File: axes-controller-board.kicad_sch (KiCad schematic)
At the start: 76 parts, among them IC1 TPS5450QDDARQ1, J10 Conn_01x08, J11 Conn_01x04, J12 Conn_01x08, J13 Conn_01x04, J14 Conn_01x08, J15 Conn_01x08, J16 Conn_01x04, J17 Conn_01x08, J18 Conn_01x08, J19 Conn_01x04, J2 Conn_01x03, J20 Conn_01x08, J21 Conn_01x08, J22 Conn_01x04, J23 Conn_01x08, J24 Conn_01x08, J25 Conn_01x04, J26 Conn_01x08, J27 Raspberry_Pi_2_3, J28 DC1, J29 DC2, J3 Conn_01x03, J30 DC3, J31 Conn_01x08, J32 Conn_01x08, J33 DC1, J34 Conn_01x08, J35 Conn_01x08, J36 Conn_01x08, J37 ENDSTOP, J38 ENDSTOP, J39 ENDSTOP, J4 Conn_01x03, J40 Conn_01x03, J41 ENDSTOP, J42 ENDSTOP, J5 DRIVER, J6 NTC, J7 DRIVER, J8 NTC, J9 Conn_01x08, U1 LM1117MP-3.3

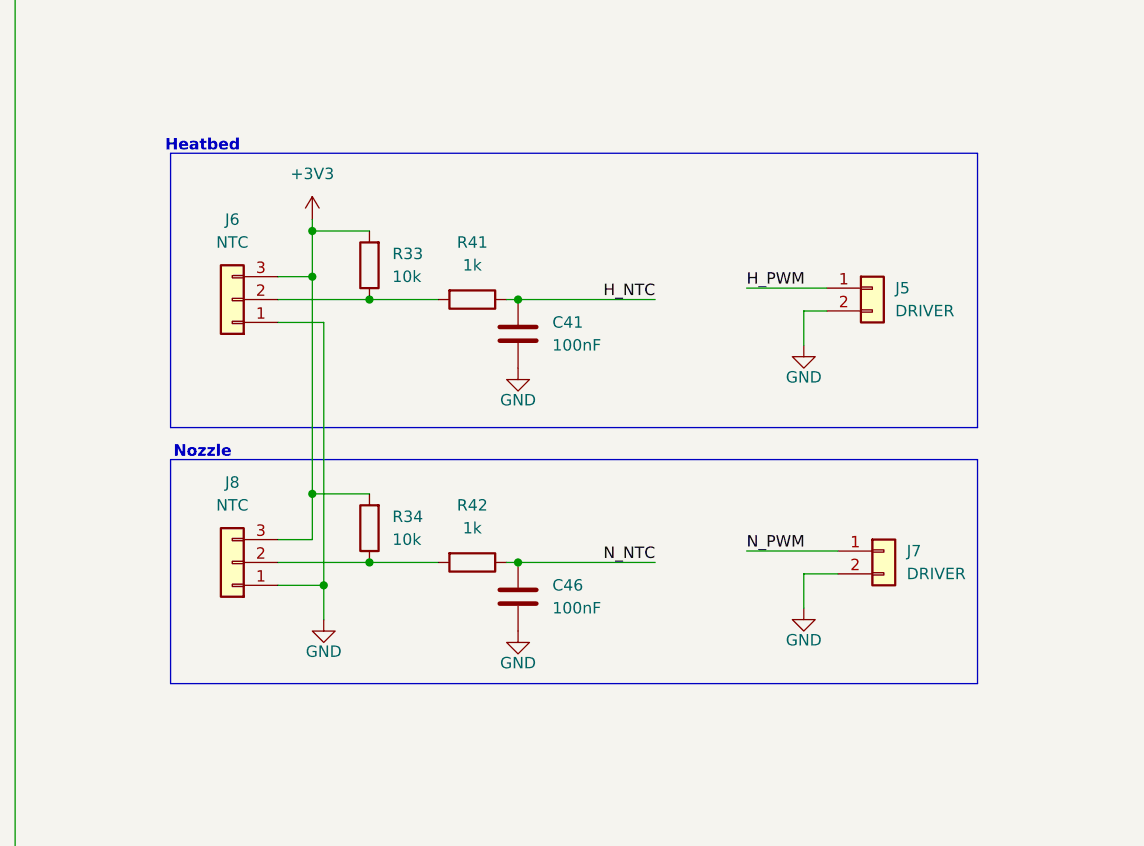
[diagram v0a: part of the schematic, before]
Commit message: fix: nozzle and hb connector
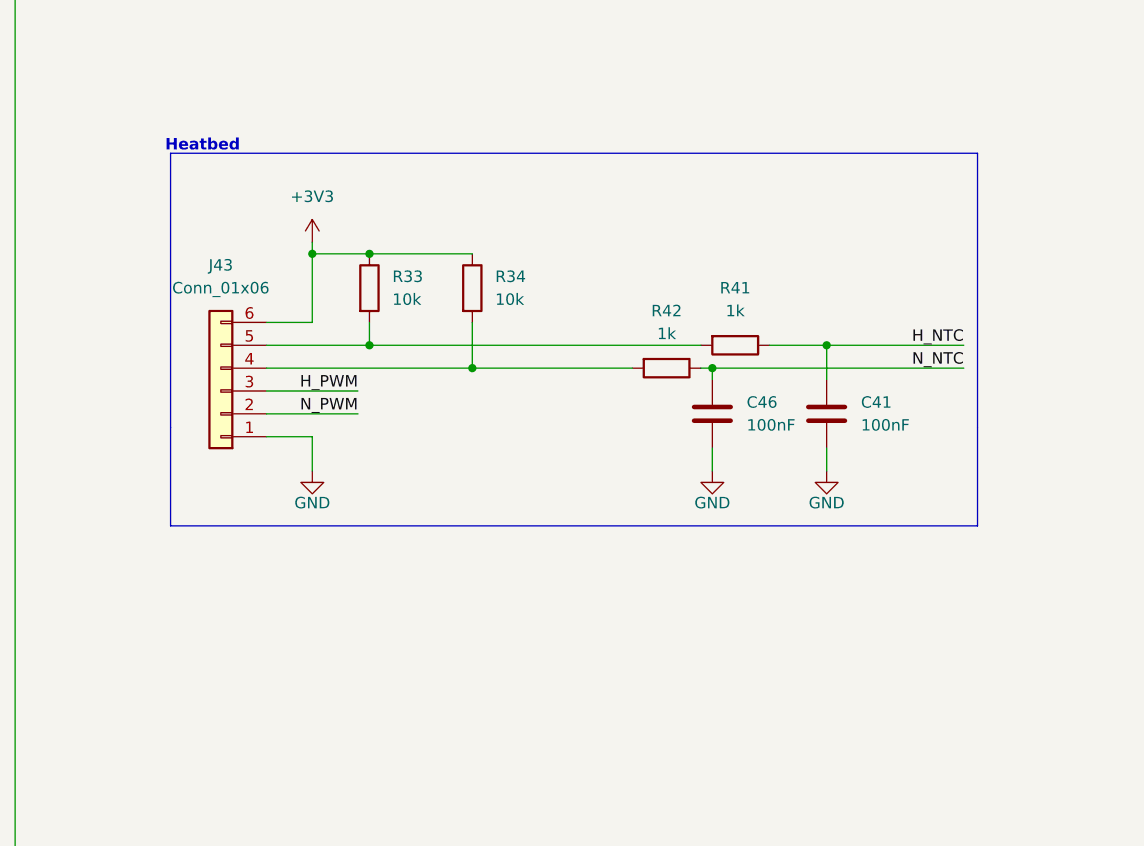
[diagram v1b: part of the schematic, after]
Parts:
- removed J5, J7: DRIVER, Connector_PinHeader_2.54mm:PinHeader_1x02_P2.54mm_Vertical, symbol Connector_Generic:Conn_01x02
- removed J6, J8: NTC, Connector_PinHeader_2.54mm:PinHeader_1x03_P2.54mm_Vertical, symbol Connector_Generic:Conn_01x03
- added J43: Conn_01x06, Local:1985234, symbol Connector_Generic:Conn_01x06
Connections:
- net +3V3: now also R33.1, R34.1, J43.6 (Pin_6); no longer R33.2, R34.2
- net GND: now also J43.1 (Pin_1)
- net H_PWM: now also J43.3 (Pin_3)
- net N_PWM: now also J43.2 (Pin_2)
- net at R41.2: now also R33.2, J43.5 (Pin_5); no longer R33.1
- net at R42.2: now also R34.2, J43.4 (Pin_4); no longer R34.1
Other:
- note removed: "Nozzle"
- moved on the sheet: C41, C46, R41, R42

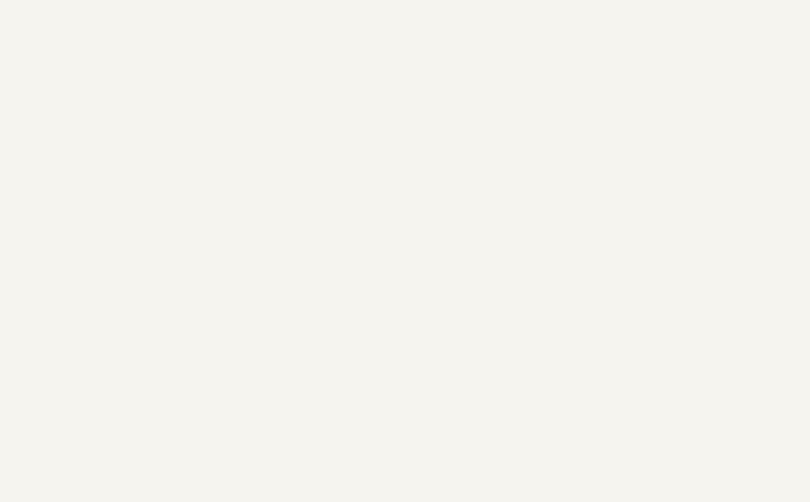
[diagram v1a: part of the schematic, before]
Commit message: feat: mounting holes
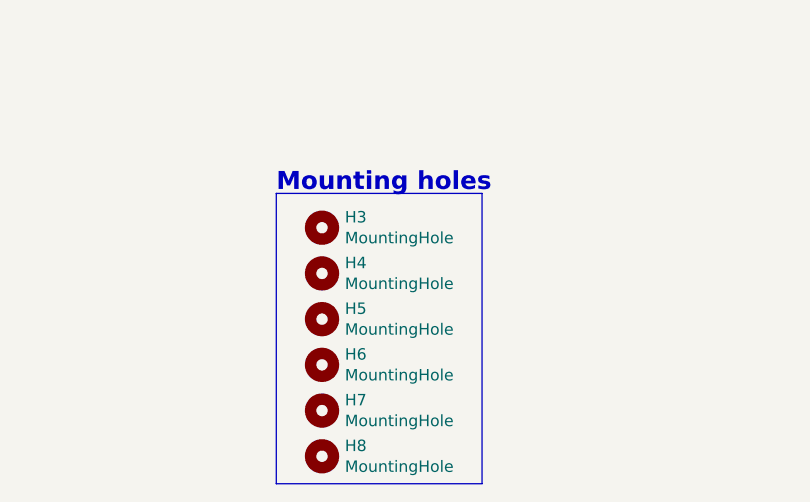
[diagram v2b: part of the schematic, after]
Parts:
- added H3, H4, H5, H6, H7, H8: MountingHole, Local:MountingHole_3.2mm_M3_ISO14580, symbol Mechanical:MountingHole
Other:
- note added: "Mounting holes"

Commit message: feat: spare pins
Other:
- moved on the sheet: H2
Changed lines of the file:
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@@
 	(polyline
 		(pts
-			(xy 341.122 66.548) (xy 341.122 20.574)
+			(xy 340.868 76.454) (xy 340.868 20.574)
 		)
 		(stroke
@@
 	(polyline
 		(pts
-			(xy 179.832 20.574) (xy 179.832 66.548)
+			(xy 179.832 20.574) (xy 179.832 76.454)
 		)
 		(stroke
@@
 	(polyline
 		(pts
-			(xy 179.832 66.548) (xy 341.122 66.548)
+			(xy 179.832 76.454) (xy 340.868 76.454)
 		)
 		(stroke
@@
 	(wire
 		(pts
-			(xy 191.77 72.39) (xy 200.66 72.39)
+			(xy 196.85 68.58) (xy 205.74 68.58)
 		)
 		(stroke
@@
 	)
 	(label "GNDM"
-		(at 200.66 72.39 180)
+		(at 205.74 68.58 180)
 		(effects
 			(font
@@
 	(symbol
 		(lib_id "Mechanical:MountingHole_Pad")
-		(at 189.23 72.39 90)
+		(at 194.31 68.58 90)
 		(unit 1)
 		(exclude_from_sim yes)
@@
 		(on_board yes)
 		(dnp no)
-		(fields_autoplaced yes)
 		(property "Reference" "H2"
-			(at 187.96 66.04 90)
+			(at 194.056 71.882 90)
 			(effects
 				(font
@@
 		)
 		(property "Value" "MountingHole_Pad"
-			(at 187.96 68.58 90)
+			(at 204.216 71.628 90)
 			(effects
 				(font
@@
 		)
 		(property "Footprint" "Local:TestPoint_GNDedge"
-			(at 189.23 72.39 0)
+			(at 194.31 68.58 0)
 			(effects
 				(font
@@
 		)
 		(property "Datasheet" "~"
-			(at 189.23 72.39 0)
+			(at 194.31 68.58 0)
 			(effects
 				(font
@@
 		)
 		(property "Description" "Mounting Hole with connection"
-			(at 189.23 72.39 0)
+			(at 194.31 68.58 0)
 			(effects
 				(font

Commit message: fix: DNPs
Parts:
- J10, J11, J12, J13, J14, J15, J16, J17, J18, J19, J20, J21, J22, J23, J24, J25, J26, J37, J38, J39, J41, J42, J9: now not fitted
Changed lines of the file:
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@@
 		(in_bom yes)
 		(on_board yes)
-		(dnp no)
+		(dnp yes)
 		(fields_autoplaced yes)
 		(property "Reference" "J41"
@@
 		(in_bom yes)
 		(on_board yes)
-		(dnp no)
+		(dnp yes)
 		(property "Reference" "J24"
 			(at 486.41 262.128 0)
@@
 		(in_bom yes)
 		(on_board yes)
-		(dnp no)
+		(dnp yes)
 		(fields_autoplaced yes)
 		(property "Reference" "J22"
@@
 		(in_bom yes)
 		(on_board yes)
-		(dnp no)
+		(dnp yes)
 		(fields_autoplaced yes)
 		(property "Reference" "J19"
@@
 		(in_bom yes)
 		(on_board yes)
-		(dnp no)
+		(dnp yes)
 		(property "Reference" "J14"
 			(at 505.206 93.726 0)
@@
 		(in_bom yes)
 		(on_board yes)
-		(dnp no)
+		(dnp yes)
 		(property "Reference" "J17"
 			(at 505.206 130.556 0)
@@
 		(in_bom yes)
 		(on_board yes)
-		(dnp no)
+		(dnp yes)
 		(property "Reference" "J20"
 			(at 505.206 167.386 0)
@@
 		(in_bom yes)
 		(on_board yes)
-		(dnp no)
+		(dnp yes)
 		(fields_autoplaced yes)
 		(property "Reference" "J39"
@@
 		(in_bom yes)
 		(on_board yes)
-		(dnp no)
+		(dnp yes)
 		(property "Reference" "J23"
 			(at 505.206 202.946 0)
@@
 		(in_bom yes)
 		(on_board yes)
-		(dnp no)
+		(dnp yes)
 		(fields_autoplaced yes)
 		(property "Reference" "J16"
@@
 		(in_bom yes)
 		(on_board yes)
-		(dnp no)
+		(dnp yes)
 		(fields_autoplaced yes)
 		(property "Reference" "J37"
@@
 		(in_bom yes)
 		(on_board yes)
-		(dnp no)
+		(dnp yes)
 		(property "Reference" "J15"
 			(at 486.41 154.178 0)
@@
 		(in_bom yes)
 		(on_board yes)
-		(dnp no)
+		(dnp yes)
 		(property "Reference" "J9"
 			(at 486.41 81.788 0)
@@
 		(in_bom yes)
 		(on_board yes)
-		(dnp no)
+		(dnp yes)
 		(property "Reference" "J12"
 			(at 486.41 117.348 0)
@@
 		(in_bom yes)
 		(on_board yes)
-		(dnp no)
+		(dnp yes)
 		(property "Reference" "J10"
 			(at 505.206 58.166 0)
@@
 		(in_bom yes)
 		(on_board yes)
-		(dnp no)
+		(dnp yes)
 		(fields_autoplaced yes)
 		(property "Reference" "J13"
@@
 		(in_bom yes)
 		(on_board yes)
-		(dnp no)
+		(dnp yes)
 		(fields_autoplaced yes)
 		(property "Reference" "J25"
@@
 		(in_bom yes)
 		(on_board yes)
-		(dnp no)
+		(dnp yes)
 		(fields_autoplaced yes)
 		(property "Reference" "J38"
@@
 		(in_bom yes)
 		(on_board yes)
-		(dnp no)
+		(dnp yes)
 		(property "Reference" "J26"
 			(at 505.206 238.506 0)
@@
 		(in_bom yes)
 		(on_board yes)
-		(dnp no)
+		(dnp yes)
 		(property "Reference" "J18"
 			(at 486.41 191.008 0)
@@
 		(in_bom yes)
 		(on_board yes)
-		(dnp no)
+		(dnp yes)
 		(fields_autoplaced yes)
 		(property "Reference" "J11"
@@
 		(in_bom yes)
 		(on_board yes)
-		(dnp no)
+		(dnp yes)
 		(fields_autoplaced yes)
 		(property "Reference" "J42"
@@
 		(in_bom yes)
 		(on_board yes)
-		(dnp no)
+		(dnp yes)
 		(property "Reference" "J21"
 			(at 486.41 226.568 0)

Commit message: feat: production codes
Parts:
- C14, J2, J28, J29, J3, J30, J31, J32, J33, J34, J35, J36, J4, J40, J43: now not fitted; now left out of the parts list
- C51, C52, C53, C54, C55, C56, J10, J11, J12, J13, J14, J15, J16, J17, J18, J19, J20, J21, J22, J23, J24, J25, J26, J37, J38, J39, J41, J42, J9: now left out of the parts list
- D3: LCSC (none) -> C72264
- IC1: LCSC (none) -> C181270
- L2: LCSC (none) -> C2847584
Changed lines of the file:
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@@
 		(unit 1)
 		(exclude_from_sim no)
-		(in_bom yes)
+		(in_bom no)
 		(on_board yes)
 		(dnp yes)
@@
 		(unit 1)
 		(exclude_from_sim no)
-		(in_bom yes)
+		(in_bom no)
 		(on_board yes)
 		(dnp yes)
@@
 		(unit 1)
 		(exclude_from_sim no)
-		(in_bom yes)
+		(in_bom no)
 		(on_board yes)
 		(dnp yes)
@@
 		(unit 1)
 		(exclude_from_sim no)
-		(in_bom yes)
+		(in_bom no)
 		(on_board yes)
 		(dnp yes)
@@
 		(unit 1)
 		(exclude_from_sim no)
-		(in_bom yes)
+		(in_bom no)
 		(on_board yes)
-		(dnp no)
+		(dnp yes)
 		(property "Reference" "J36"
 			(at 40.386 205.486 0)
@@
 		(unit 1)
 		(exclude_from_sim no)
-		(in_bom yes)
+		(in_bom no)
 		(on_board yes)
-		(dnp no)
+		(dnp yes)
 		(property "Reference" "J28"
 			(at 39.878 246.888 0)
@@
 		(unit 1)
 		(exclude_from_sim no)
-		(in_bom yes)
+		(in_bom no)
 		(on_board yes)
-		(dnp no)
+		(dnp yes)
 		(property "Reference" "J30"
 			(at 39.878 262.128 0)
@@
 		(unit 1)
 		(exclude_from_sim no)
-		(in_bom yes)
+		(in_bom no)
 		(on_board yes)
 		(dnp yes)
@@
 		(unit 1)
 		(exclude_from_sim no)
-		(in_bom yes)
+		(in_bom no)
 		(on_board yes)
 		(dnp yes)
@@
 		(unit 1)
 		(exclude_from_sim no)
-		(in_bom yes)
+		(in_bom no)
 		(on_board yes)
 		(dnp yes)
@@
 		(unit 1)
 		(exclude_from_sim no)
-		(in_bom yes)
+		(in_bom no)
 		(on_board yes)
 		(dnp yes)
@@
 		(unit 1)
 		(exclude_from_sim no)
-		(in_bom yes)
+		(in_bom no)
 		(on_board yes)
 		(dnp yes)
@@
 		(unit 1)
 		(exclude_from_sim no)
-		(in_bom yes)
+		(in_bom no)
 		(on_board yes)
 		(dnp yes)
@@
 		(unit 1)
 		(exclude_from_sim no)
-		(in_bom yes)
+		(in_bom no)
 		(on_board yes)
 		(dnp yes)
@@
 		(unit 1)
 		(exclude_from_sim no)
-		(in_bom yes)
+		(in_bom no)
 		(on_board yes)
-		(dnp no)
+		(dnp yes)
 		(fields_autoplaced yes)
 		(property "Reference" "J4"
@@
 		(unit 1)
 		(exclude_from_sim no)
-		(in_bom yes)
+		(in_bom no)
 		(on_board yes)
-		(dnp no)
+		(dnp yes)
 		(property "Reference" "J34"
 			(at 40.386 152.146 0)
@@
 		(unit 1)
 		(exclude_from_sim no)
-		(in_bom yes)
+		(in_bom no)
 		(on_board yes)
-		(dnp no)
+		(dnp yes)
 		(fields_autoplaced yes)
 		(property "Reference" "J3"
@@
 		(unit 1)
 		(exclude_from_sim no)
-		(in_bom yes)
+		(in_bom no)
 		(on_board yes)
 		(dnp yes)
@@
 		(unit 1)
 		(exclude_from_sim no)
-		(in_bom yes)
+		(in_bom no)
 		(on_board yes)
 		(dnp yes)
@@
 		(unit 1)
 		(exclude_from_sim no)
-		(in_bom yes)
+		(in_bom no)
 		(on_board yes)
 		(dnp yes)
@@
 			)
 		)
+		(property "LCSC" "C2847584"
+			(at 295.91 29.21 90)
+			(effects
+				(font
+					(size 1.27 1.27)
+				)
+				(hide yes)
+			)
+		)
 		(pin "1"
 		)
@@
 		(unit 1)
 		(exclude_from_sim no)
-		(in_bom yes)
+		(in_bom no)
 		(on_board yes)
 		(dnp yes)
@@
 		(unit 1)
 		(exclude_from_sim no)
-		(in_bom yes)
+		(in_bom no)
 		(on_board yes)
 		(dnp yes)
@@
 		(unit 1)
 		(exclude_from_sim no)
-		(in_bom yes)
+		(in_bom no)
 		(on_board yes)
 		(dnp yes)
@@
 		(unit 1)
 		(exclude_from_sim no)
-		(in_bom yes)
+		(in_bom no)
 		(on_board yes)
-		(dnp no)
+		(dnp yes)
 		(fields_autoplaced yes)
 		(property "Reference" "J40"
@@
 			)
 		)
+		(property "LCSC" "C72264"
+			(at 290.83 34.29 90)
+			(effects
+				(font
+					(size 1.27 1.27)
+				)
+				(hide yes)
+			)
+		)
 		(pin "1"
 		)
@@
 		(unit 1)
 		(exclude_from_sim no)
-		(in_bom yes)
+		(in_bom no)
 		(on_board yes)
-		(dnp no)
+		(dnp yes)
 		(property "Reference" "J32"
 			(at 134.366 255.016 0)
@@
 		(unit 1)
 		(exclude_from_sim no)
-		(in_bom yes)
+		(in_bom no)
 		(on_board yes)
 		(dnp yes)
@@
 		(unit 1)
 		(exclude_from_sim no)
-		(in_bom yes)
+		(in_bom no)
 		(on_board yes)
-		(dnp no)
+		(dnp yes)
 		(fields_autoplaced yes)
 		(property "Reference" "J43"
@@
 		(unit 1)
 		(exclude_from_sim no)
-		(in_bom yes)
+		(in_bom no)
 		(on_board yes)
-		(dnp no)
+		(dnp yes)
 		(property "Reference" "J31"
 			(at 134.366 289.306 0)
@@
 		(unit 1)
 		(exclude_from_sim no)
-		(in_bom yes)
+		(in_bom no)
 		(on_board yes)
 		(dnp yes)
@@
 		(unit 1)
 		(exclude_from_sim no)
-		(in_bom yes)
+		(in_bom no)
 		(on_board yes)
 		(dnp yes)
@@
 		(unit 1)
 		(exclude_from_sim no)
-		(in_bom yes)
+		(in_bom no)
 		(on_board yes)
 		(dnp yes)
@@
 			)
 		)
+		(property "LCSC" "C181270"
+			(at 236.22 39.37 0)
+			(effects
+				(font
+					(size 1.27 1.27)
+				)
+				(hide yes)
+			)
+		)
 		(pin "9"
 		)
@@
 		(unit 1)
 		(exclude_from_sim no)
-		(in_bom yes)
+		(in_bom no)
 		(on_board yes)
 		(dnp yes)
@@
 		(unit 1)
 		(exclude_from_sim no)
-		(in_bom yes)
+		(in_bom no)
 		(on_board yes)
 		(dnp yes)
@@
 		(unit 1)
 		(exclude_from_sim no)
-		(in_bom yes)
+		(in_bom no)
 		(on_board yes)
 		(dnp yes)
@@
 		(unit 1)
 		(exclude_from_sim no)
-		(in_bom yes)
+		(in_bom no)
 		(on_board yes)
-		(dnp no)
+		(dnp yes)
 		(property "Reference" "J33"
 			(at 183.388 43.942 0)
@@
 		(unit 1)
 		(exclude_from_sim no)
-		(in_bom yes)
+		(in_bom no)
 		(on_board yes)
-		(dnp no)
+		(dnp yes)
 		(property "Reference" "J35"
 			(at 40.386 178.816 0)
@@
 		(unit 1)
 		(exclude_from_sim no)
-		(in_bom yes)
+		(in_bom no)
 		(on_board yes)
 		(dnp yes)
@@
 		(unit 1)
 		(exclude_from_sim no)
-		(in_bom yes)
+		(in_bom no)
 		(on_board yes)
 		(dnp yes)
@@
 		(unit 1)
 		(exclude_from_sim no)
-		(in_bom yes)
+		(in_bom no)
 		(on_board yes)
-		(dnp no)
+		(dnp yes)
 		(fields_autoplaced yes)
 		(property "Reference" "J2"
@@
 		(unit 1)
 		(exclude_from_sim no)
-		(in_bom yes)
+		(in_bom no)
 		(on_board yes)
 		(dnp yes)
@@
 		(unit 1)
 		(exclude_from_sim no)
-		(in_bom yes)
+		(in_bom no)
 		(on_board yes)
 		(dnp yes)
@@
 		(unit 1)
 		(exclude_from_sim no)
-		(in_bom yes)
+		(in_bom no)
 		(on_board yes)
-		(dnp no)
+		(dnp yes)
 		(property "Reference" "J29"
 			(at 39.878 254.508 0)
@@
 		(unit 1)
 		(exclude_from_sim no)
-		(in_bom yes)
+		(in_bom no)
 		(on_board yes)
 		(dnp yes)
@@
 		(unit 1)
 		(exclude_from_sim no)
-		(in_bom yes)
+		(in_bom no)
 		(on_board yes)
-		(dnp no)
+		(dnp yes)
 		(fields_autoplaced yes)
 		(property "Reference" "C14"

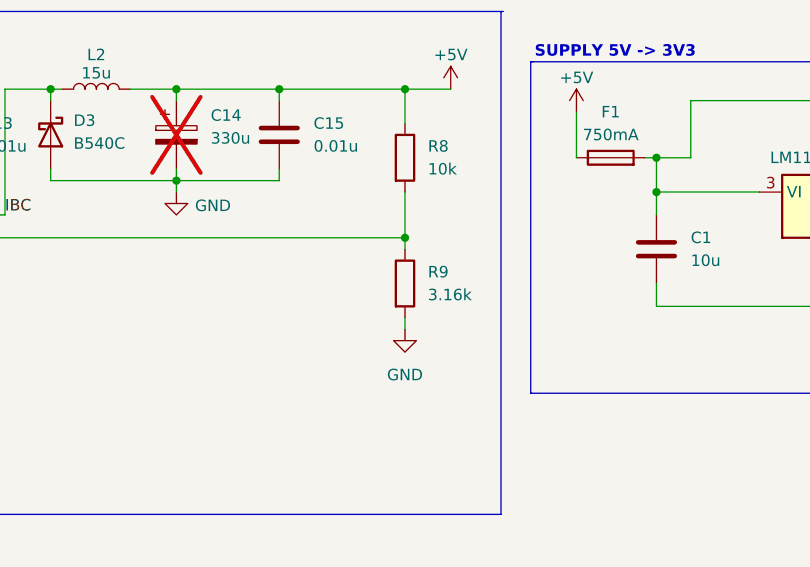
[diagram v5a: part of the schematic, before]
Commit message: fix: root sheet LCSC codes
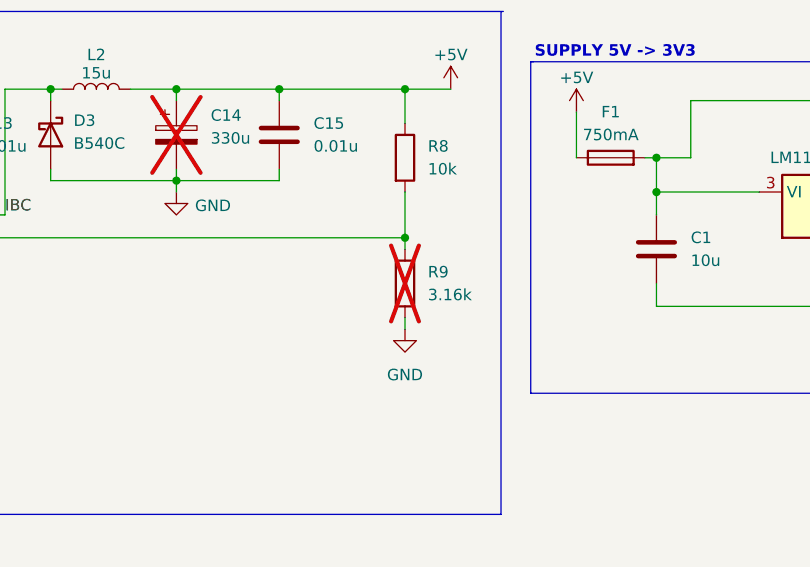
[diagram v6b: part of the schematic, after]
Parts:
- C1, C12, C13, C15, C2, C3: LCSC (none) -> C57112
- C10, C11: LCSC (none) -> C2918489
- C41, C46: LCSC (none) -> C14663
- R1: LCSC (none) -> C22975
- R2, R41, R42: LCSC (none) -> C21190
- R33, R34, R8: LCSC (none) -> C25804
- R9: LCSC (none) -> C22993; now not fitted; now left out of the parts list
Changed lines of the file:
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@@
 			)
 		)
+		(property "LCSC" "C2918489"
+			(at 199.39 45.72 0)
+			(effects
+				(font
+					(size 1.27 1.27)
+				)
+				(hide yes)
+			)
+		)
 		(pin "2"
 		)
@@
 			)
 		)
+		(property "LCSC" "C25804"
+			(at 293.37 283.21 0)
+			(effects
+				(font
+					(size 1.27 1.27)
+				)
+				(hide yes)
+			)
+		)
 		(pin "2"
 		)
@@
 			)
 		)
+		(property "LCSC" "C21190"
+			(at 422.91 40.64 0)
+			(effects
+				(font
+					(size 1.27 1.27)
+				)
+				(hide yes)
+			)
+		)
 		(pin "2"
 		)
@@
 			)
 		)
+		(property "LCSC" "C57112"
+			(at 223.52 45.72 0)
+			(effects
+				(font
+					(size 1.27 1.27)
+				)
+				(hide yes)
+			)
+		)
 		(pin "2"
 		)
@@
 			)
 		)
+		(property "LCSC" "C57112"
+			(at 279.4 34.29 0)
+			(effects
+				(font
+					(size 1.27 1.27)
+				)
+				(hide yes)
+			)
+		)
 		(pin "2"
 		)
@@
 			)
 		)
+		(property "LCSC" "C14663"
+			(at 331.47 297.18 0)
+			(effects
+				(font
+					(size 1.27 1.27)
+				)
+				(hide yes)
+			)
+		)
 		(pin "2"
 		)
@@
 			)
 		)
+		(property "LCSC" "C25804"
+			(at 304.8 283.21 0)
+			(effects
+				(font
+					(size 1.27 1.27)
+				)
+				(hide yes)
+			)
+		)
 		(pin "2"
 		)
@@
 		(unit 1)
 		(exclude_from_sim no)
-		(in_bom yes)
+		(in_bom no)
 		(on_board yes)
-		(dnp no)
+		(dnp yes)
 		(fields_autoplaced yes)
 		(property "Reference" "R9"
@@
 			)
 		)
+		(property "LCSC" "C22993"
+			(at 330.2 50.8 0)
+			(effects
+				(font
+					(size 1.27 1.27)
+				)
+				(hide yes)
+			)
+		)
 		(pin "2"
 		)
@@
 			)
 		)
+		(property "LCSC" "C57112"
+			(at 401.32 46.99 0)
+			(effects
+				(font
+					(size 1.27 1.27)
+				)
+				(hide yes)
+			)
+		)
 		(pin "1"
 		)
@@
 			)
 		)
+		(property "LCSC" "C21190"
+			(at 334.01 289.56 90)
+			(effects
+				(font
+					(size 1.27 1.27)
+				)
+				(hide yes)
+			)
+		)
 		(pin "2"
 		)
@@
 			)
 		)
+		(property "LCSC" "C22975"
+			(at 412.75 40.64 0)
+			(effects
+				(font
+					(size 1.27 1.27)
+				)
+				(hide yes)
+			)
+		)
 		(pin "1"
 		)
@@
 			)
 		)
+		(property "LCSC" "C21190"
+			(at 326.39 292.1 90)
+			(effects
+				(font
+					(size 1.27 1.27)
+				)
+				(hide yes)
+			)
+		)
 		(pin "2"
 		)
@@
 			)
 		)
+		(property "LCSC" "C57112"
+			(at 316.23 34.29 0)
+			(effects
+				(font
+					(size 1.27 1.27)
+				)
+				(hide yes)
+			)
+		)
 		(pin "2"
 		)
@@
 			)
 		)
+		(property "LCSC" "C14663"
+			(at 344.17 297.18 0)
+			(effects
+				(font
+					(size 1.27 1.27)
+				)
+				(hide yes)
+			)
+		)
 		(pin "2"
 		)
@@
 			)
 		)
+		(property "LCSC" "C2918489"
+			(at 210.82 45.72 0)
+			(effects
+				(font
+					(size 1.27 1.27)
+				)
+				(hide yes)
+			)
+		)
 		(pin "2"
 		)
@@
 			)
 		)
+		(property "LCSC" "C25804"
+			(at 330.2 36.83 0)
+			(effects
+				(font
+					(size 1.27 1.27)
+				)
+				(hide yes)
+			)
+		)
 		(pin "2"
 		)
@@
 			)
 		)
+		(property "LCSC" "C57112"
+			(at 358.14 46.99 0)
+			(effects
+				(font
+					(size 1.27 1.27)
+				)
+				(hide yes)
+			)
+		)
 		(pin "1"
 		)
@@
 			(at 392.43 46.99 0)
 			(effects
+				(font
+					(size 1.27 1.27)
+				)
+				(hide yes)
+			)
+		)
+		(property "LCSC" "C57112"
+			(at 392.43 46.99 0)
+			(effects
